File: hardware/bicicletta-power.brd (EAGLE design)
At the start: 160 x 100 mm, 23 parts, among them IC1 LM5017, IC2 LM1117-3.3

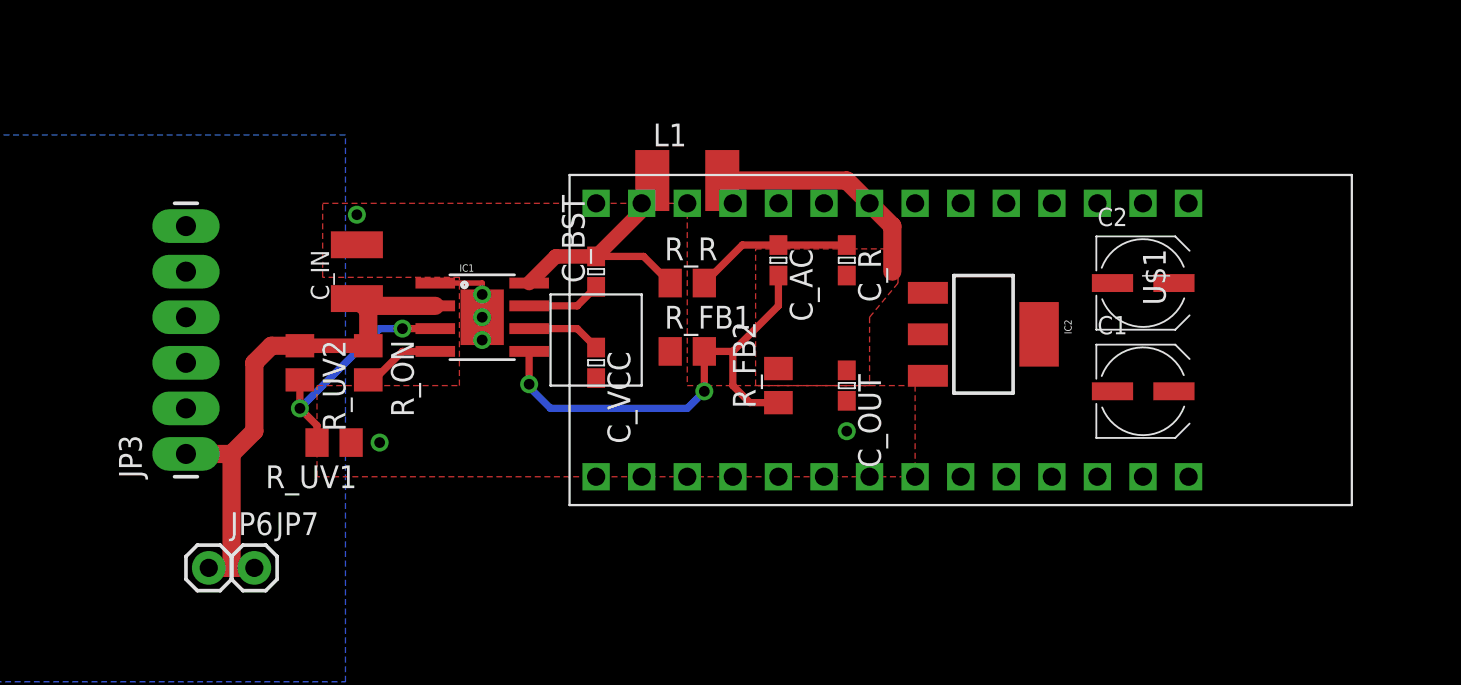
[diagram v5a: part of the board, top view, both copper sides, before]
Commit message: Rethinking the PCB layout to be more compact.
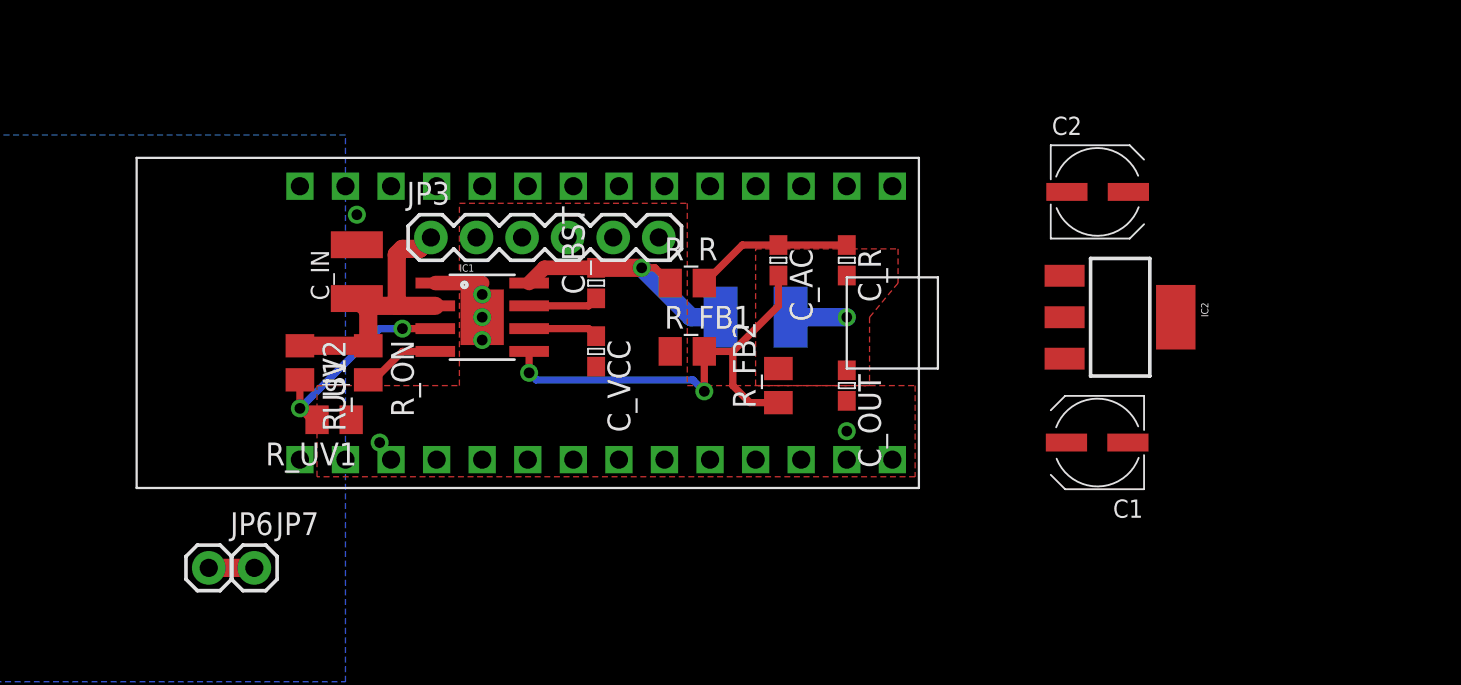
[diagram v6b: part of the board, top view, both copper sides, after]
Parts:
- JP3: device SparkFun-Connectors:1X06_LONGPADS -> SparkFun-Connectors:1X06
- moved U$1 24.1 mm to (55.9, 73.3), turned to 90 degrees
- moved JP3 18.2 mm to (50.5, 78.1), turned to 0 degrees
- moved L1 8.52 mm to (68.6, 73.7), flipped to the bottom, turned to 180 degrees
- moved IC2 7.68 mm to (88.9, 73.7)
- moved C2 5.68 mm to (87.6, 80.6)
- moved C1 3.82 mm to (87.6, 66.7), turned to 180 degrees
- moved R_UV1 1.27 mm to (45.1, 67.9)
- moved C_BST 0.64 mm to (59.7, 75.6)
- moved C_VCC 0.63 mm to (59.7, 71.8)
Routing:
- net V_BATT: track 31.2 -> 18.9 mm
- net 5V: track 13.1 -> 3.13 mm, vias 0 -> 1
- net N$2: track 26.6 -> 25.3 mm
- net N$3: track 13.3 -> 12.6 mm
- net N$4: track 14.6 -> 14.1 mm, vias 0 -> 1

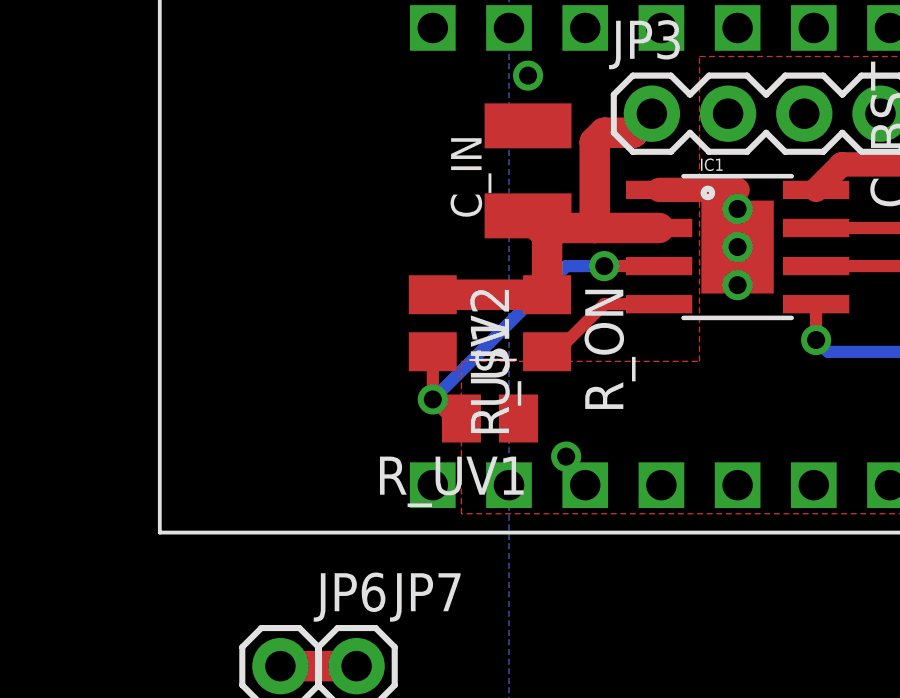
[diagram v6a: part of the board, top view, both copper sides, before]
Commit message: More compact still. Need to check solderability.
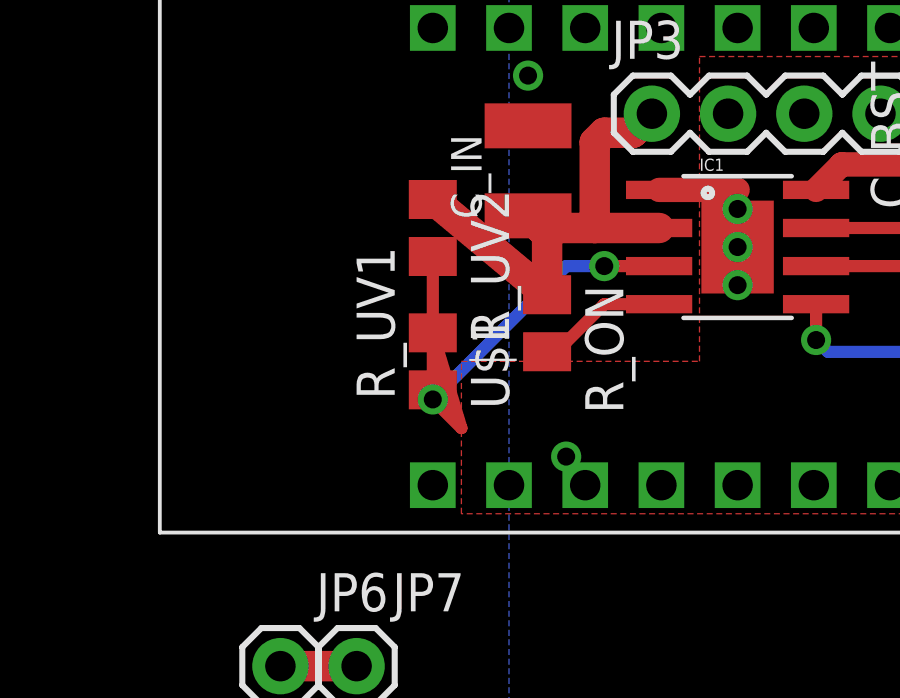
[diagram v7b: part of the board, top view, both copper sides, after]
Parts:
- moved R_UV2 3.17 mm to (43.2, 74.3)
- moved R_UV1 2.69 mm to (43.2, 69.8), turned to 90 degrees
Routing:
- net N$3: track 12.6 -> 18.8 mm
- net V_BATT: track 18.9 -> 20.1 mm
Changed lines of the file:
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@@
 <element name="C_IN" library="rcl" package="C1210K" value="2.2uF" x="46.355" y="76.2" rot="R90"/>
 <element name="C_OUT" library="rcl" package="C0603" value="5.6uF" x="73.66" y="69.85" rot="R270"/>
-<element name="R_UV2" library="rcl" package="M0805" value="125K" x="43.18" y="71.12" rot="R270"/>
-<element name="R_UV1" library="rcl" package="M0805" value="14K" x="45.085" y="67.945" rot="R180"/>
+<element name="R_UV2" library="rcl" package="M0805" value="125K" x="43.18" y="74.295" rot="R270"/>
+<element name="R_UV1" library="rcl" package="M0805" value="14K" x="43.18" y="69.85" rot="R90"/>
 <element name="L1" library="rcl" package="L1812" value="100uH" x="68.58" y="73.66" rot="MR180"/>
 <element name="R_R" library="rcl" package="M0805" value="2M" x="64.77" y="75.565"/>
@@
 <contactref element="JP6" pad="1"/>
 <contactref element="JP7" pad="1"/>
-<wire x1="43.18" y1="72.07" x2="46.99" y2="72.07" width="1.016" layer="1"/>
+<wire x1="43.18" y1="75.245" x2="46.99" y2="72.07" width="1.016" layer="1"/>
 <wire x1="46.99" y1="72.07" x2="46.99" y2="74.065" width="1.016" layer="1"/>
 <wire x1="46.99" y1="74.065" x2="46.355" y2="74.7" width="1.016" layer="1"/>
@@
 <wire x1="48.895" y1="77.47" x2="48.5775" y2="77.1525" width="1.016" layer="1"/>
 <wire x1="48.5775" y1="77.1525" x2="48.5775" y2="74.295" width="1.016" layer="1"/>
-<wire x1="40.64" y1="59.69" x2="43.18" y2="72.07" width="0" layer="19" extent="1-1"/>
+<wire x1="40.64" y1="59.69" x2="43.18" y2="75.245" width="0" layer="19" extent="1-1"/>
 </signal>
 <signal name="5V">
@@
 <wire x1="47.625" y1="73.025" x2="43.18" y2="68.58" width="0.4064" layer="16"/>
 <via x="43.18" y="68.58" extent="1-16" drill="0.6"/>
-<wire x1="44.135" y1="67.945" x2="44.135" y2="67.625" width="0.4064" layer="1"/>
+<wire x1="43.18" y1="70.8" x2="44.135" y2="67.625" width="0.4064" layer="1"/>
 <wire x1="44.135" y1="67.625" x2="43.18" y2="68.58" width="0.4064" layer="1"/>
-<wire x1="43.18" y1="70.17" x2="43.18" y2="68.58" width="0.4064" layer="1"/>
+<wire x1="43.18" y1="73.345" x2="43.18" y2="68.58" width="0.4064" layer="1"/>
 </signal>
 <signal name="3.3V">

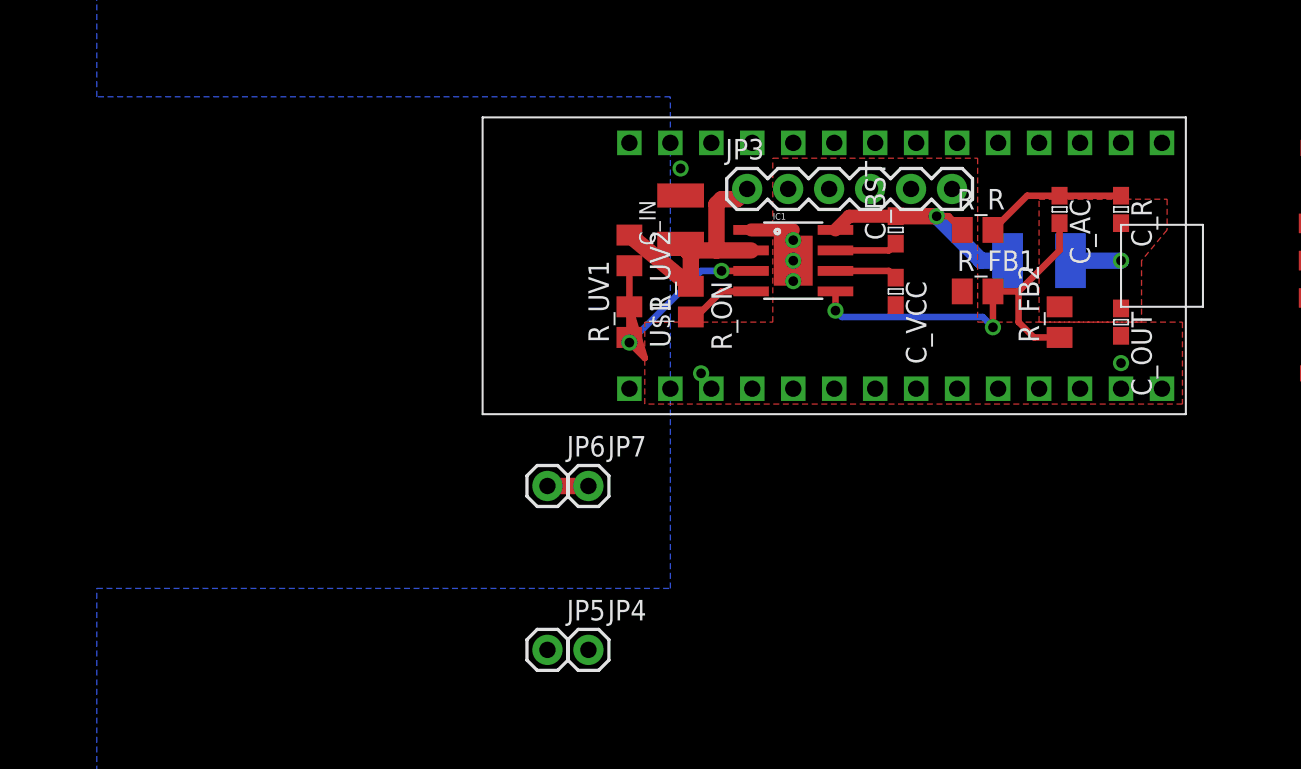
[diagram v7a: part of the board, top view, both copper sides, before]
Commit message: Layout of switching regulator is nearing finalization.
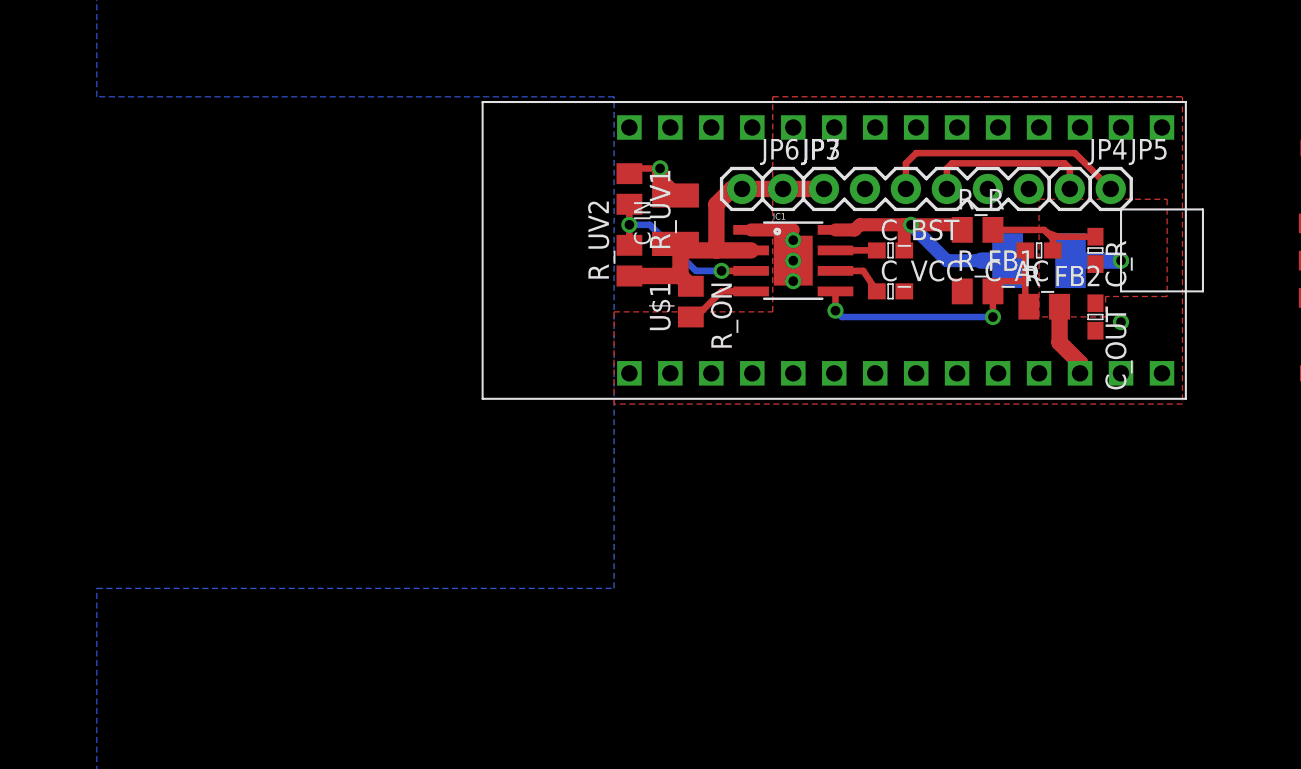
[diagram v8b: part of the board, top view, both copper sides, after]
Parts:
- moved JP5 45.1 mm to (73.0, 78.1)
- moved JP4 41.3 mm to (70.5, 78.1)
- moved JP6 22.0 mm to (50.2, 78.1)
- moved JP7 22.0 mm to (52.7, 78.1)
- moved R_UV1 8.26 mm to (43.2, 78.1), turned to 270 degrees
- moved JP3 4.76 mm to (55.2, 78.1)
- moved C_R 3.00 mm to (72.1, 74.3)
- moved C_AC 2.84 mm to (68.6, 74.3), turned to 180 degrees
- moved C_OUT 1.62 mm to (72.1, 70.2)
- moved R_FB2 1.35 mm to (68.9, 70.8), turned to 0 degrees
- moved C_BST 1.31 mm to (59.4, 74.3), turned to 0 degrees
- moved U$1 0.95 mm to (55.9, 74.3)
- moved R_UV2 0.64 mm to (43.2, 73.7), turned to 90 degrees
- moved C_IN 0.32 mm to (46.0, 76.2)
- moved C_VCC 0.32 mm to (59.4, 71.8), turned to 0 degrees
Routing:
- net SHUNT-: track 0.00 -> 15.5 mm
- net SHUNT+: track 0.00 -> 10.4 mm
- net N$3: track 18.8 -> 11.3 mm
- net N$2: track 25.3 -> 18.9 mm
- net 5V: track 3.13 -> 7.78 mm
- net GND: track 3.25 -> 7.55 mm, vias 6 -> 5
- net N$4: track 14.1 -> 17.0 mm
- net N$7: track 3.91 -> 2.57 mm
- net N$6: track 8.82 -> 7.73 mm
- net V_BATT: track 20.1 -> 21.0 mm
- net N$9: track 3.91 -> 3.25 mm
